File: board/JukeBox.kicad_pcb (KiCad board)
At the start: 2 copper layers, 78.5 x 80 mm, 56 parts, among them J1 USB_C_Receptacle_USB2.0, J2 Conn_01x02, J3 Conn_01x04, J4 Conn_01x03, SW1 SW_SPST, SW10 SW_SPST, SW11 SW_SPST, SW12 SW_SPST, SW2 SW_SPST, SW3 SW_SPST, SW4 SW_SPST, SW5 SW_SPST, SW6 SW_SPST, SW7 SW_SPST, SW8 SW_SPST, SW9 SW_SPST, U1 ATmega8U2-A, Y1 16MHz

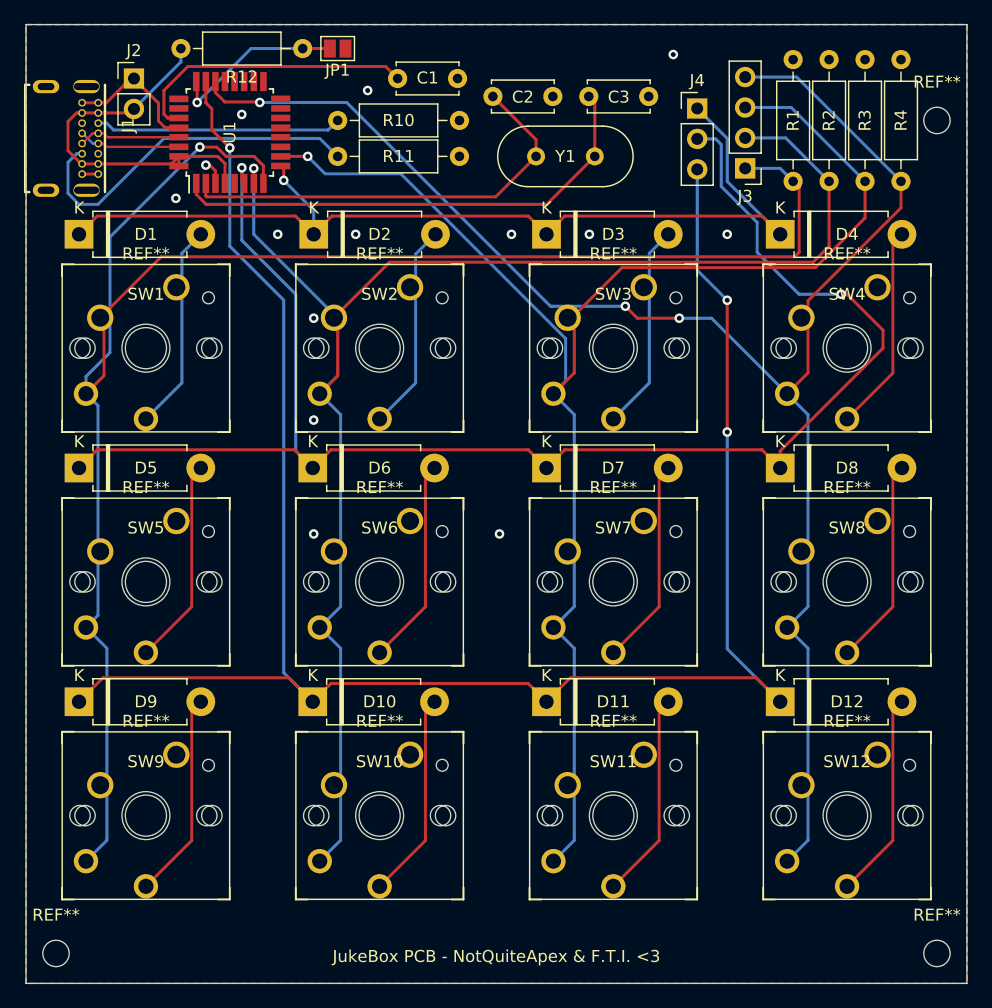
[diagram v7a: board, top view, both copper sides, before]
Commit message: fix all traces for dual sockets
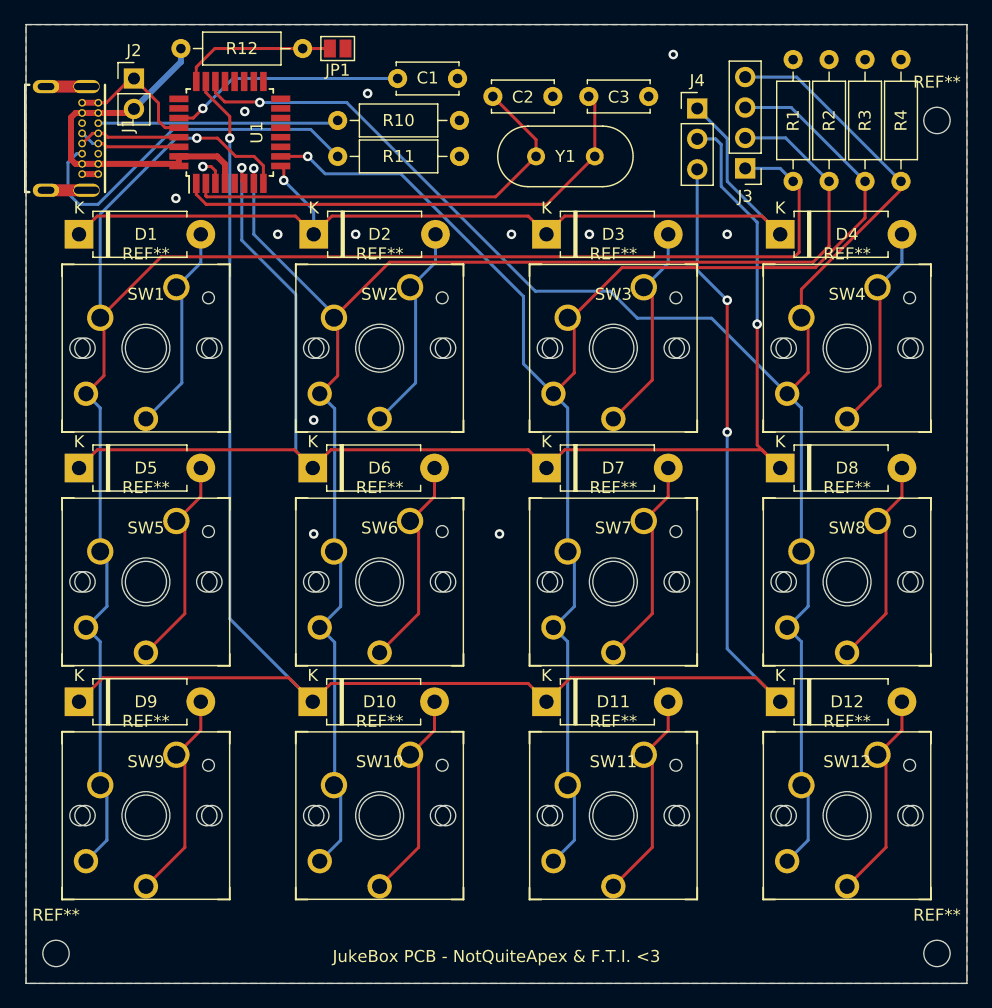
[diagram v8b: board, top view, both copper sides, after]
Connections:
- REF** pad 1: (no net) -> Net-(D7-Pad2)
- REF** pad 2: (no net) -> COL_3 (x3)
- REF** pad 1: (no net) -> Net-(D5-Pad2)
- REF** pad 2: (no net) -> COL_1 (x3)
- REF** pad 1: (no net) -> Net-(D10-Pad2)
- REF** pad 2: (no net) -> COL_2 (x3)
- REF** pad 1: (no net) -> Net-(D9-Pad2)
- REF** pad 1: (no net) -> Net-(D2-Pad2)
- REF** pad 1: (no net) -> Net-(D11-Pad2)
- REF** pad 1: (no net) -> Net-(D12-Pad2)
- REF** pad 2: (no net) -> COL_4 (x3)
- REF** pad 1: (no net) -> Net-(D1-Pad2)
- REF** pad 1: (no net) -> Net-(D6-Pad2)
- REF** pad 1: (no net) -> Net-(D3-Pad2)
- REF** pad 1: (no net) -> Net-(D8-Pad2)
- REF** pad 1: (no net) -> Net-(D4-Pad2)
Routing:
- net ROW_2: track 131.9 -> 122.4 mm
- net GND: track 15.0 -> 22.0 mm, vias 14 -> 13
- net COL_2: track 130.0 -> 123.1 mm
- net Net-(C1-Pad2): track 24.1 -> 19.6 mm, vias 0 -> 1
- net COL_1: track 151.2 -> 147.2 mm
- net Net-(D8-Pad2): track 17.3 -> 19.0 mm
- net Net-(D6-Pad2): track 17.3 -> 19.0 mm
- net Net-(D7-Pad2): track 17.3 -> 19.0 mm
- net Net-(D5-Pad2): track 17.3 -> 19.0 mm
- net Net-(JP1-Pad2): track 14.7 -> 13.1 mm, vias 1 -> 0
- net COL_3: track 127.5 -> 126.6 mm
- net Net-(J1-PadB5): track 29.8 -> 30.5 mm
- net Net-(D11-Pad2): track 17.3 -> 17.9 mm
- net Net-(D10-Pad2): track 17.3 -> 17.9 mm
- net Net-(D12-Pad2): track 17.3 -> 17.9 mm
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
